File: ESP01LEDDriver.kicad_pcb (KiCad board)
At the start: 2 copper layers, 53.3 x 49.5 mm, 20 parts, among them CON1 POWERLJACK, J1 Conn_01x04, J2 Conn_02x04_Odd_Even, J3 Screw_Terminal_01x03, J4 USB_B, Q1 2N7002, SW1 RESETBUTTON, U1 AZ1117-3.3

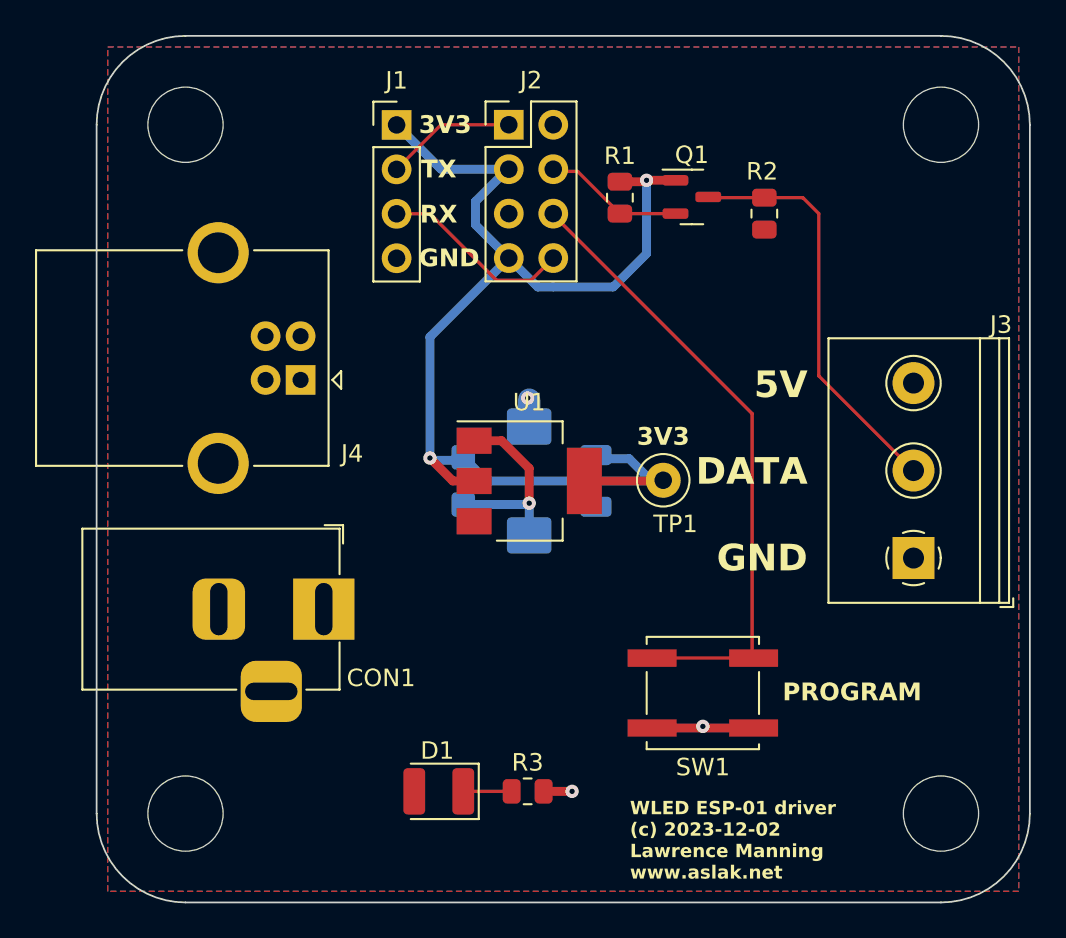
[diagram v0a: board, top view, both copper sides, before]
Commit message: v2: added an FTDI IC for programming the ESP01 in place
This part is optional: if included on a built up board then the ESP01 can
be programmed without removing it from the board or using a USB UART
attached to the header pins.

Thanks to Phil Mehew (www.mehew.net) for this suggestion!
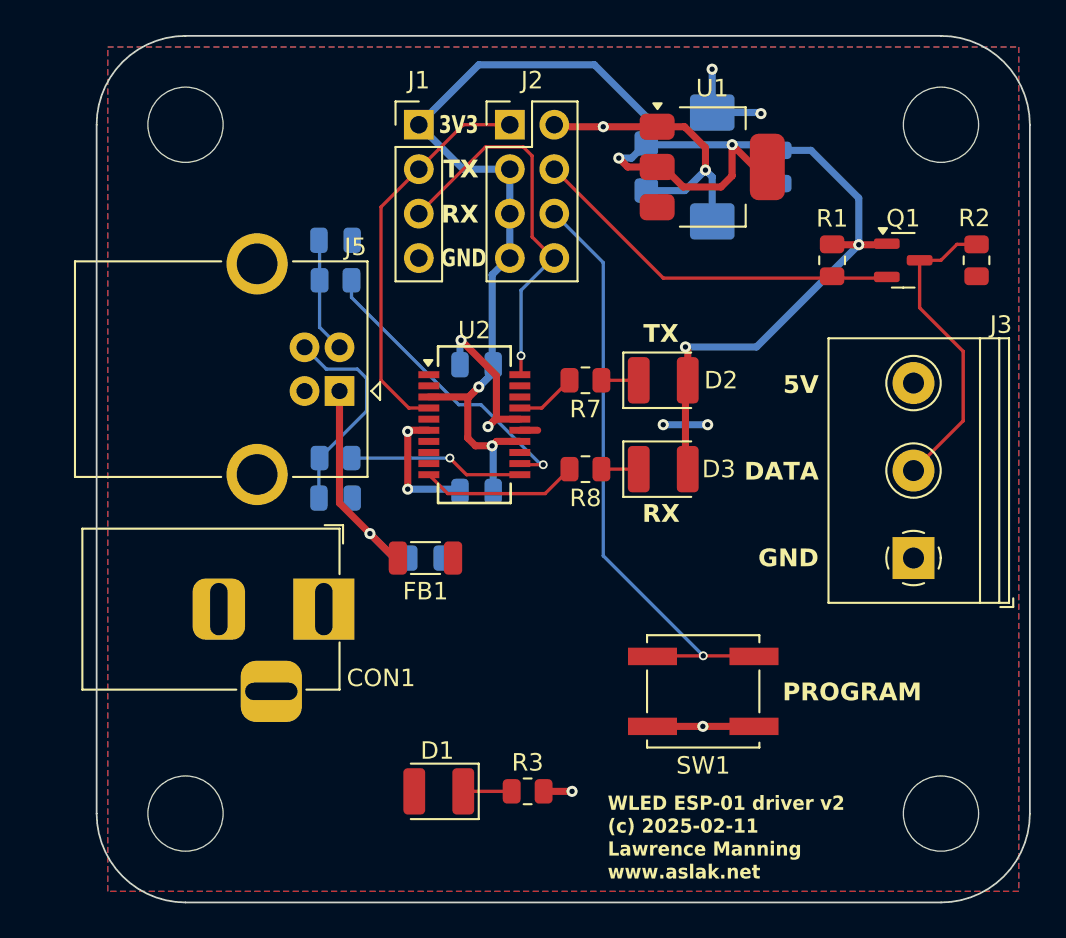
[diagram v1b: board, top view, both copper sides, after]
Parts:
- removed J4: USB_B, Connector_USB:USB_B_OST_USB-B1HSxx_Horizontal
- removed TP1: 3V3, TestPoint:TestPoint_Loop_D1.80mm_Drill1.0mm_Beaded
- added C4: 10n, Capacitor_SMD:C_0805_2012Metric, B.Cu at (31.5, 46.4)
- added C5: 47p, Capacitor_SMD:C_0805_2012Metric, B.Cu at (26.4, 28.2)
- added C6: 47p, Capacitor_SMD:C_0805_2012Metric, B.Cu at (26.4, 42.9)
- added C7: 4.7u, Capacitor_SMD:C_0805_2012Metric, B.Cu at (34.4, 35.3)
- added C8: 4.7u, Capacitor_SMD:C_0805_2012Metric, B.Cu at (34.4, 42.5)
- added D2: UART_LED, LED_SMD:LED_1210_3225Metric, F.Cu at (45.1, 36.2)
- added D3: UART_LED, LED_SMD:LED_1210_3225Metric, F.Cu at (45.1, 41.3)
- added FB1: Bead, Inductor_SMD:L_1206_3216Metric, F.Cu at (31.5, 46.4)
- added J5: USB_B, Connector_USB:USB_B_OST_USB-B1HSxx_Horizontal, F.Cu at (26.6, 36.8)
- added R5: 27, Resistor_SMD:R_0805_2012Metric, B.Cu at (26.4, 30.5)
- added R6: 27, Resistor_SMD:R_0805_2012Metric, B.Cu at (26.4, 40.6)
- added R7: 1K, Resistor_SMD:R_0805_2012Metric, F.Cu at (40.6, 36.2)
- added R8: 1K, Resistor_SMD:R_0805_2012Metric, F.Cu at (40.6, 41.3)
- added U2: FT231XS, Package_SO:SSOP-20_3.9x8.7mm_P0.635mm, F.Cu at (34.3, 38.7)
- C2: footprint Capacitor_SMD:C_1206_3216Metric -> Capacitor_SMD:C_0805_2012Metric
- moved C1 20.8 mm to (47.9, 24.0)
- moved C2 20.8 mm to (51.7, 24.0)
- moved C3 20.8 mm to (44.1, 24.0)
- moved U1 20.8 mm to (47.9, 24.0)
- moved R1 12.6 mm to (54.7, 29.3)
- moved Q1 12.6 mm to (58.8, 29.3)
- moved R2 12.4 mm to (63.0, 29.3)
- moved J1 1.27 mm to (31.1, 21.6)
- moved SW1 0.10 mm to (47.4, 54.0)
- moved J2 0.06 mm to (36.3, 21.6)
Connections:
- J2 pad 5: /RST -> +3V3
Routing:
- net +3V3: track 68.5 -> 102.5 mm, vias 2 -> 6
- net GND: track 18.9 -> 43.1 mm, vias 3 -> 8
- net Net-(U2-USBDM): track 0.00 -> 17.3 mm, vias 0 -> 1
- net /UART_TX: track 7.47 -> 22.6 mm
- net /VBUS: track 0.00 -> 13.9 mm, vias 0 -> 1
- net /GPIO2: track 7.98 -> 21.7 mm
- net Net-(J5-D+): track 0.00 -> 12.3 mm
- net /UART_RX: track 11.1 -> 22.1 mm, vias 0 -> 1
- net Net-(U2-USBDP): track 0.00 -> 10.0 mm, vias 0 -> 1
- net /RXLED: track 0.00 -> 9.06 mm
- net +5V: track 1.54 -> 8.85 mm, vias 1 -> 4
- net Net-(J5-D-): track 0.00 -> 6.60 mm
- net Net-(J3-Pin_2): track 23.6 -> 18.0 mm
- net /TXLED: track 0.00 -> 3.50 mm
- net Net-(D3-K): track 0.00 -> 2.13 mm
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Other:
- board text added: "WLED ESP-01 driver v2 (c) 2025-02-11 Lawrence Manning www.aslak.net"
- board text removed: "WLED ESP-01 driver (c) 2023-12-02 Lawrence Manning www.aslak.net"
